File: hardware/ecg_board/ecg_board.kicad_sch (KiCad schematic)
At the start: 53 parts, among them J1 USB_C_Receptacle_USB2.0_16P, J3 MEM2075-00-140-01-A, Q1 PMOS, U1 ESP32-S3-WROOM-1, U2 TLV75801PDBV, U3 AD8232, U4 MCP73832-2-OT, U5 USBLC6-2P6

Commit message: updated schematic and finish pcb v1
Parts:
- added BT1: Battery_Cell, Battery:battery_pads, symbol Device:Battery_Cell
- added SW1: SW_SPDT, Button_Switch_SMD:SW_SPDT_PCM12, symbol Switch:SW_SPDT
- C10, C12, C13, C14: footprint Capacitor_SMD:C_0603_1608Metric -> Capacitor_SMD:C_0805_2012Metric
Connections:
- net +5V: no longer C12.2, U2.1 (IN), U2.3 (EN)
- net +BATT: now also BT1.1 (+), SW1.2 (B); no longer C14.2, D1.2, Q1.1 (D), U4.3 (V_{BAT})
- net CS_SD: now also U1.9 (IO16); no longer U1.26 (IO45)
- net GND: now also BT1.2 (-)
- net MISO: now also U1.6 (IO6); no longer U1.34 (IO41)
- net MOSI: now also U1.8 (IO15); no longer U1.35 (IO42)
- net SCK: now also U1.7 (IO7); no longer U1.33 (IO40)
- net VDD: now also C12.2, U2.1 (IN), U2.3 (EN)
- net at J1.A7 (D-): now also J1.B7 (D-), U5.3 (I/O2); no longer U5.4 (I/O2)
- net at J1.A6 (D+): now also J1.B6 (D+), U5.4 (I/O2)
- net at R2.1: now also J1.A5 (CC1)
- net at R1.1: now also J1.B5 (CC2)
- net RL renamed LL
- new net: C14.2, D1.2, Q1.1 (D), SW1.1 (A), U4.3 (V_{BAT})
- no-connect marks 8 -> 9

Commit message: added components and created bom
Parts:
- added C16, C17: 220nF, Capacitor_SMD:C_0603_1608Metric, symbol Device:C_Small
- added R23: 470k, Resistor_SMD:R_0603_1608Metric, symbol Device:R_Small
- added R25: 220k, Resistor_SMD:R_0603_1608Metric, symbol Device:R_Small
- BT1, E1, E2, E3, J3, R19, R9: now not fitted
- C1: value 0.33uF -> 100nF; LCSC Part # (none) -> C14663
- C10, C12, C13: LCSC Part # (none) -> CL10A106KP8NNNC
- C11, C15, C2, C3, C9: LCSC Part # (none) -> C14663
- C14: footprint Capacitor_SMD:C_0805_2012Metric -> Capacitor_SMD:C_0603_1608Metric; LCSC Part # (none) -> C15849
- C4: value 1.5nF -> 1nF; LCSC Part # (none) -> C1588
- C5, C6: LCSC Part # (none) -> C57112
- C7: value 0.33uF -> 100nF; LCSC Part # (none) -> C107070
- C8: LCSC Part # (none) -> C15849
- D1: LCSC Part # (none) -> C2828464
- D3: LCSC Part # (none) -> C2286
- J1: footprint Connector_USB:USB_C_Receptacle_GCT_USB4105-xx-A_16P_TopMnt_Horizontal -> Connector_USB:USB_C_Receptacle_HCTL_HC-TYPE-C-16P-01A; LCSC Part # (none) -> C2927038
- Q1: value PMOS -> NX3008PBK,215; LCSC Part # (none) -> C131670
- R1, R2, R21: LCSC Part # (none) -> C23186
- R10, R12, R13, R26: LCSC Part # (none) -> C22935
- R11: LCSC Part # (none) -> C25803
- R14: value 360k -> 220k; LCSC Part # (none) -> C22961
- R15, R16: value 180k -> 220k; LCSC Part # (none) -> C22961
- R17, R18, R3, R4, R6, R7: LCSC Part # (none) -> C7250
- R20, R8: LCSC Part # (none) -> C21189
- R22: LCSC Part # (none) -> C25804
- R24: LCSC Part # (none) -> C22975
- R27: LCSC Part # (none) -> 0603WAF2003T5E
- R5: value 1.4M -> 1M; LCSC Part # (none) -> C22935
- SW1: LCSC Part # (none) -> C109335
- U1: LCSC Part # (none) -> C2913197
- U2: LCSC Part # (none) -> C2877852
- U3: LCSC Part # (none) -> C652575
- U4: LCSC Part # (none) -> C38066
- U5: LCSC Part # (none) -> C2827693
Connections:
- net LL: now also R25.1; no longer R14.1
- net REFOUT: now also C17.2
- net at C1.1, U3.1 (HPDRIVE): now also C16.1
- net at C1.2, R3.1, U3.20 (HPSENSE): now also C16.2
- net at C7.1, R19.2, U3.6 (SW): now also C17.1, R23.2; no longer R5.2
- new net: R14.1, R25.2
- new net: R23.1, R5.2
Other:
- moved on the sheet: C1, C7

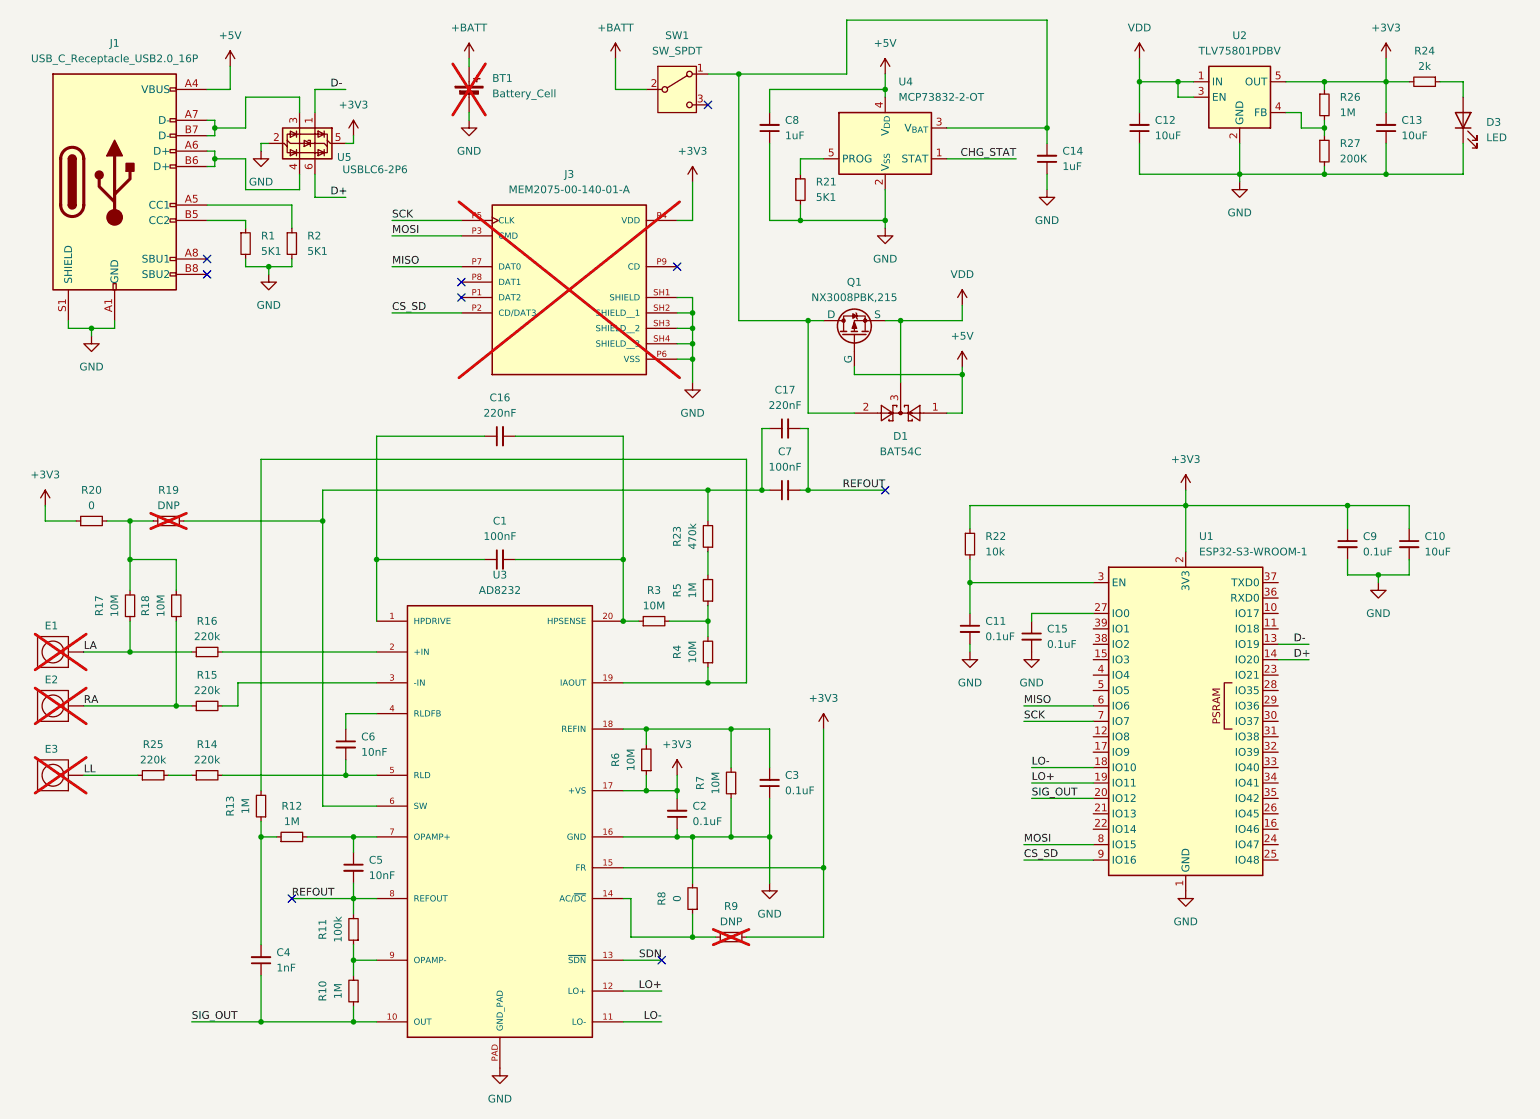
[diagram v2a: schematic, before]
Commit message: moved switch and fixed bom
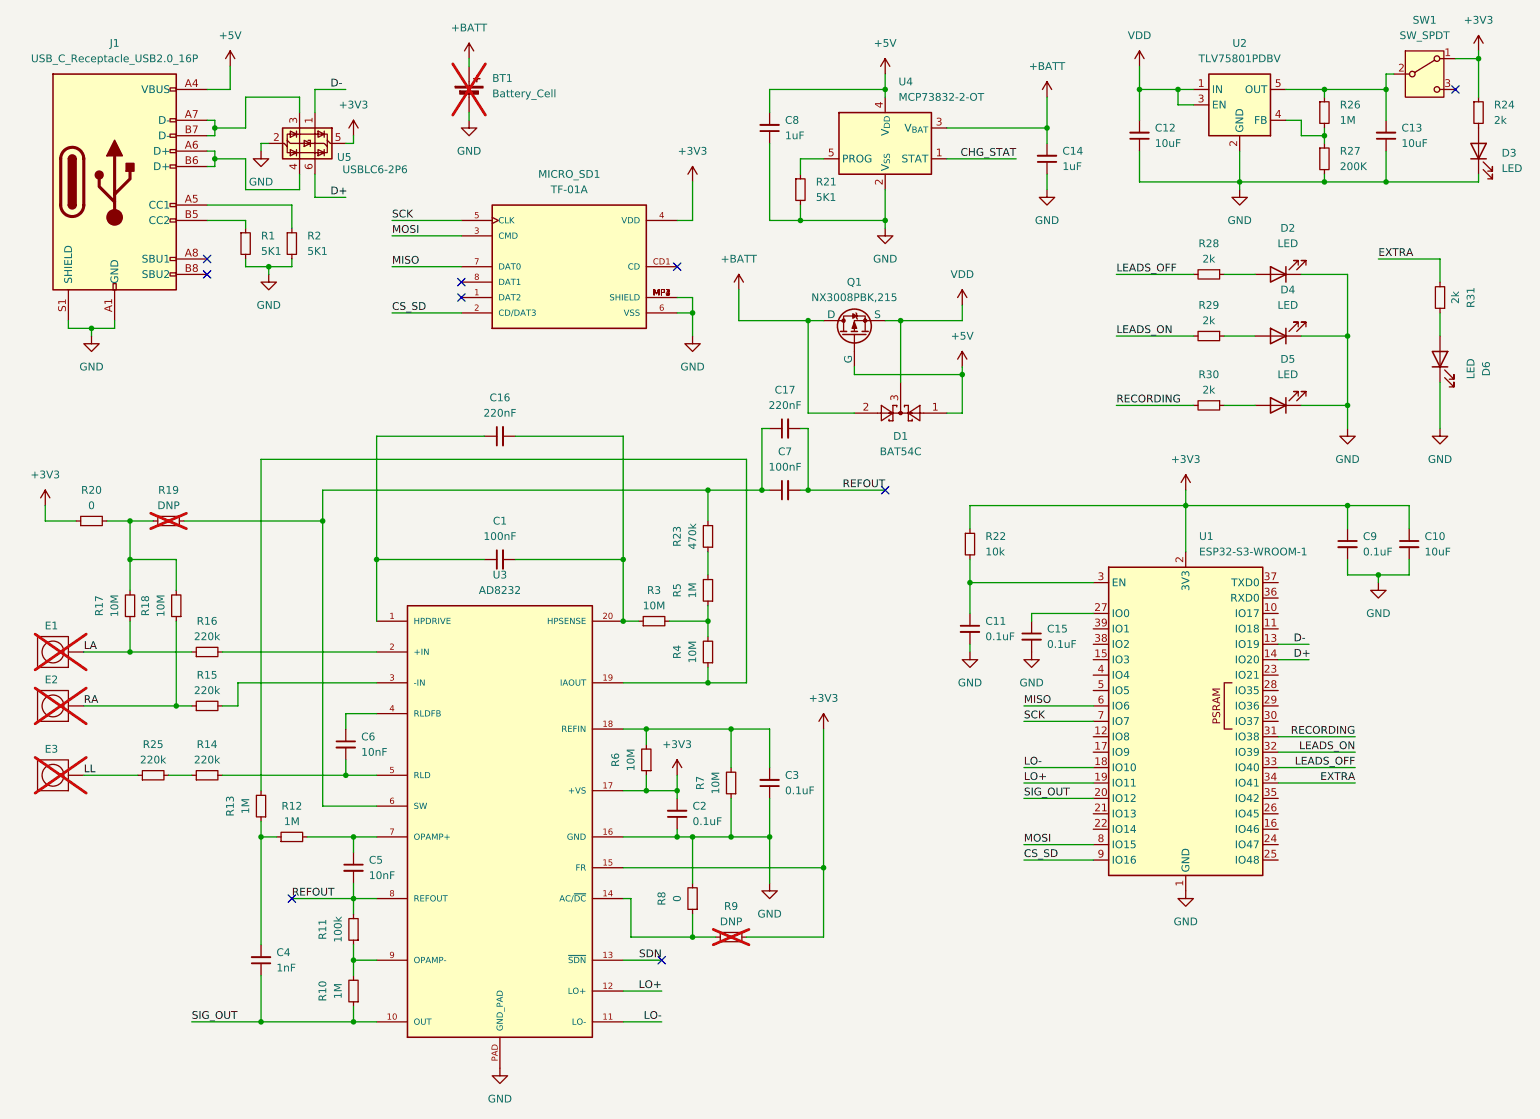
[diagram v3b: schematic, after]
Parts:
- removed J3: MEM2075-00-140-01-A, MEM2075_00_140_01_A:GCT_MEM2075-00-140-01-A, symbol MEM2075-00-140-01-A:MEM2075-00-140-01-A
- added D2, D4, D5, D6: LED, LED_SMD:LED_0603_1608Metric, symbol Device:LED
- added MICRO_SD1: TF-01A, TF-01A:TF-01A, symbol TF-01A:TF-01A
- added R28, R29, R30, R31: 2k, Resistor_SMD:R_0603_1608Metric, symbol Device:R_Small
- C10, C12, C13: LCSC Part # CL10A106KP8NNNC -> C19702
- C7: LCSC Part # C107070 -> C14663
- Q1: LCSC Part # C131670 -> C131670
- R10, R12, R13, R26, R5: LCSC Part # C22935 -> C22935
- R23: LCSC Part # C23178 -> C23178
- R27: LCSC Part # 0603WAF2003T5E -> C25811
- SW1: LCSC Part # C109335 -> C109335
- U1: LCSC Part # C2913197 -> C2913197
- U3: LCSC Part # C652575 -> C43216
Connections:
- net +3V3: now also R24.1, SW1.1 (A), MICRO_SD1.4 (VDD); no longer C13.2, R24.2, R26.1, U2.5 (OUT)
- net +BATT: now also C14.2, D1.2, Q1.1 (D), U4.3 (V_{BAT}); no longer SW1.2 (B)
- net CS_SD: now also MICRO_SD1.2 (CD/DAT3)
- net GND: now also D2.1 (K), D4.1 (K), D5.1 (K), D6.1 (K), MICRO_SD1.6 (VSS), MICRO_SD1.MP1 (SHIELD), MICRO_SD1.MP2 (SHIELD), MICRO_SD1.MP3 (SHIELD), MICRO_SD1.MP4 (SHIELD)
- net MISO: now also MICRO_SD1.7 (DAT0)
- net MOSI: now also MICRO_SD1.3 (CMD)
- net SCK: now also MICRO_SD1.5 (CLK)
- net at D3.2 (A): now also R24.2; no longer R24.1
- net RECORDING: now reaches U1.31 (IO38)
- net RECORDING: now also R30.2
- net LEADS_ON: now reaches U1.32 (IO39)
- net LEADS_ON: now also R29.2
- net LEADS_OFF: now reaches U1.33 (IO40)
- net LEADS_OFF: now also R28.2
- net EXTRA: now reaches U1.34 (IO41)
- net EXTRA: now also R31.2
- new net: D5.2 (A), R30.1
- new net: C13.2, R26.1, SW1.2 (B), U2.5 (OUT)
- new net: D6.2 (A), R31.1
- new net: D2.2 (A), R28.1
- new net: D4.2 (A), R29.1
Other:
- moved on the sheet: C12, C13, D3, R24, R26, R27, U2

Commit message: added debugging pads
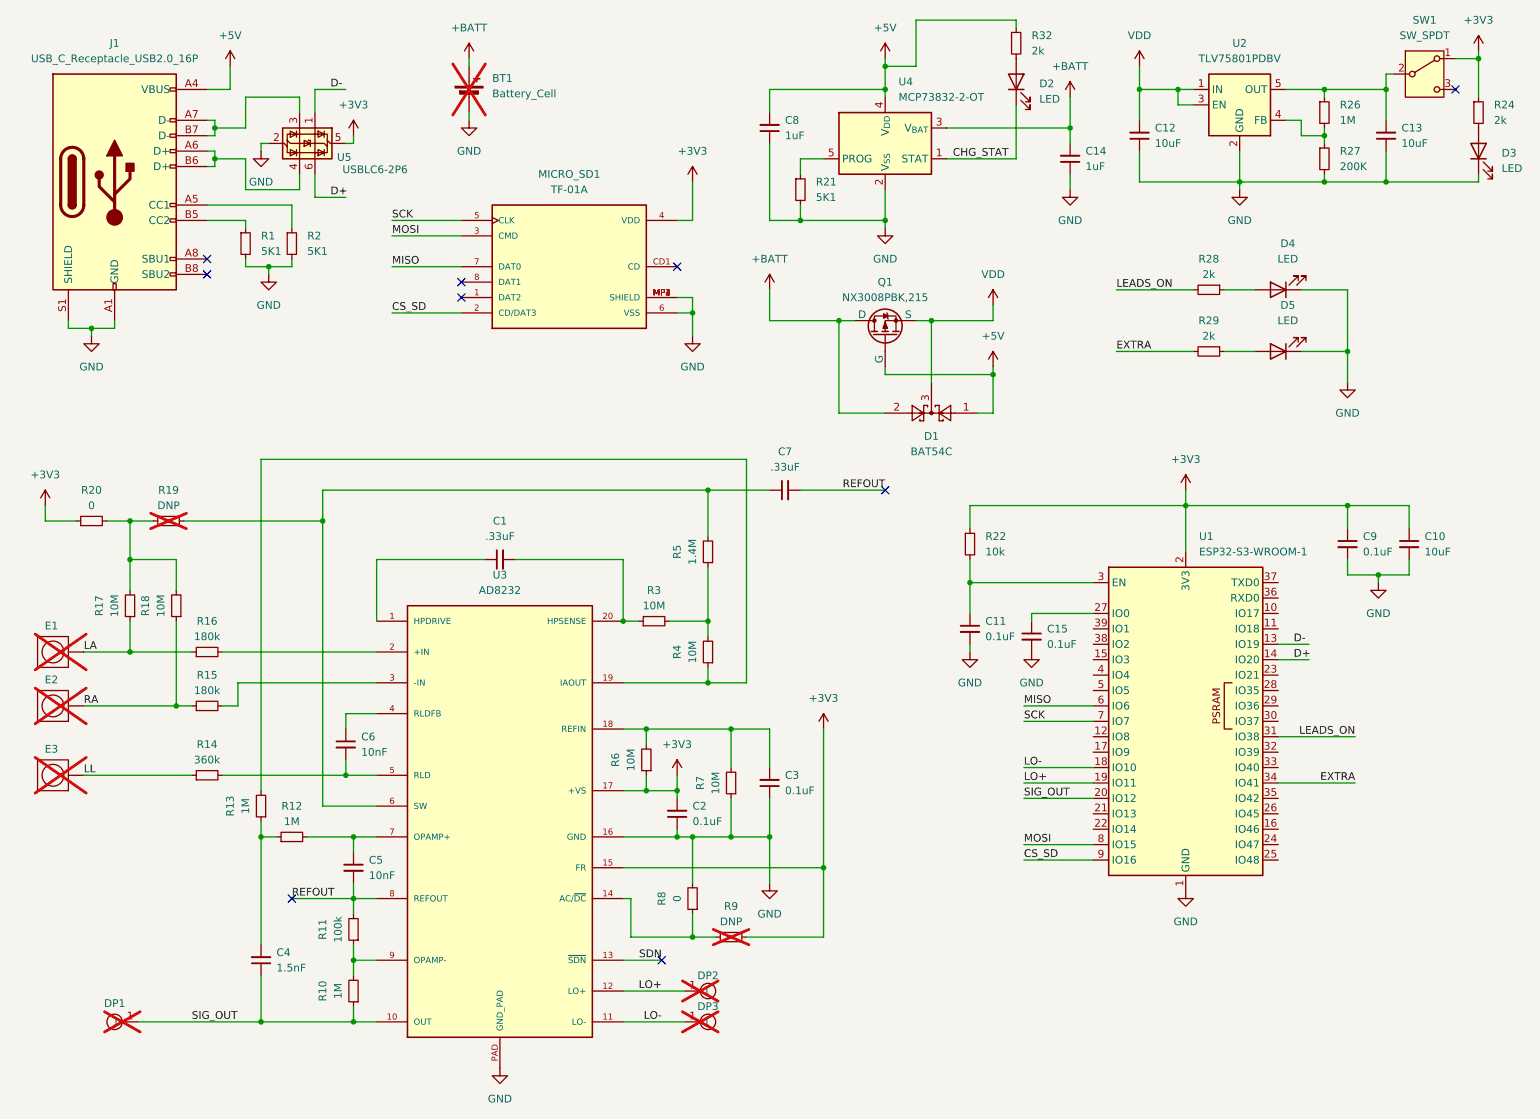
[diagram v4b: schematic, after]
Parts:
- removed C16, C17: 220nF, Capacitor_SMD:C_0603_1608Metric, symbol Device:C_Small
- removed D6: LED, LED_SMD:LED_0603_1608Metric, symbol Device:LED
- removed R23: 470k, Resistor_SMD:R_0603_1608Metric, symbol Device:R_Small
- removed R25: 220k, Resistor_SMD:R_0603_1608Metric, symbol Device:R_Small
- removed R30, R31: 2k, Resistor_SMD:R_0603_1608Metric, symbol Device:R_Small
- added DP1, DP2, DP3: ~, DebugPad:DebugPad, symbol DebugPad:DebugPadSmall
- added R32: 2k, Resistor_SMD:R_0603_1608Metric, symbol Device:R_Small
- C1, C7: value 100nF -> .33uF; LCSC Part # C14663 -> C2991452
- C4: value 1nF -> 1.5nF
- D4: LCSC Part # C434423 -> C2286
- D5: LCSC Part # C2286 -> C5123548
- R14: value 220k -> 360k; LCSC Part # C22961 -> C3016408
- R15, R16: value 220k -> 180k; LCSC Part # C22961 -> C325602
- R5: value 1M -> 1.4M; LCSC Part # C22935 -> C3016282
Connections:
- net RECORDING is gone; now on net LEADS_ON: U1.31 (IO38)
- net +5V: now also R32.1
- net CHG_STAT: now also D2.1 (K)
- net EXTRA: now also R29.2
- net GND: no longer D2.1 (K)
- net LEADS_ON: now also R28.2; no longer R29.2, U1.32 (IO39)
- net LL: now also R14.1
- net LO+: now also DP2.1
- net LO-: now also DP3.1
- net SIG_OUT: now also DP1.1
- net at D5.2 (A): now also R29.1
- net at R5.2: now also C7.1, R19.2, U3.6 (SW)
- net at D2.2 (A): now also R32.2; no longer R28.1
- net at D4.2 (A): now also R28.1; no longer R29.1
- net LEADS_OFF: no longer names the net of U1.33 (IO40)
- net LEADS_OFF: no longer R28.2
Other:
- moved on the sheet: C14, D1, Q1, R28, R29, R5
